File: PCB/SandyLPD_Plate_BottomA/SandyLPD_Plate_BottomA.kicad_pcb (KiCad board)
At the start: 2 copper layers, 131 x 83 mm, 147 parts, among them J1 Conn_02x02_Odd_Even, J2 Conn_01x03, J4 Conn_01x10_Pin, J5 USB_C_Receptacle_USB2.0, J6 USB_C_Receptacle_USB2.0, SW1 BOOT_ALT, SW2 RESET_ALT, SW3 SW_DIP_x04, U1 NCP1117-3.3_SOT223, U3 RP2040, U4 W25Q128JVPIQ, Y1 12MHz

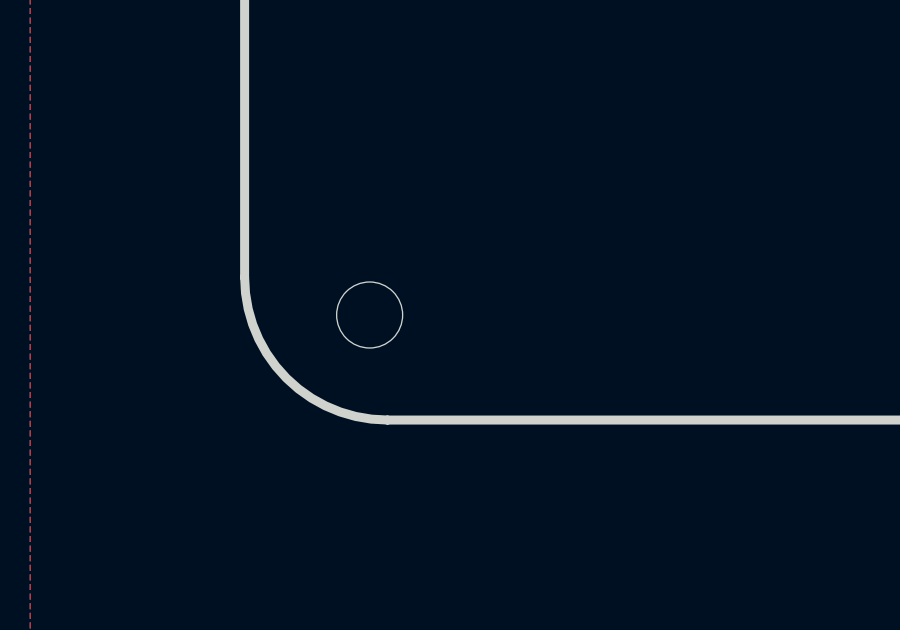
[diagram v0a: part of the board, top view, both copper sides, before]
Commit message: 基板外側のボトム用ネジ位置を変更 #18
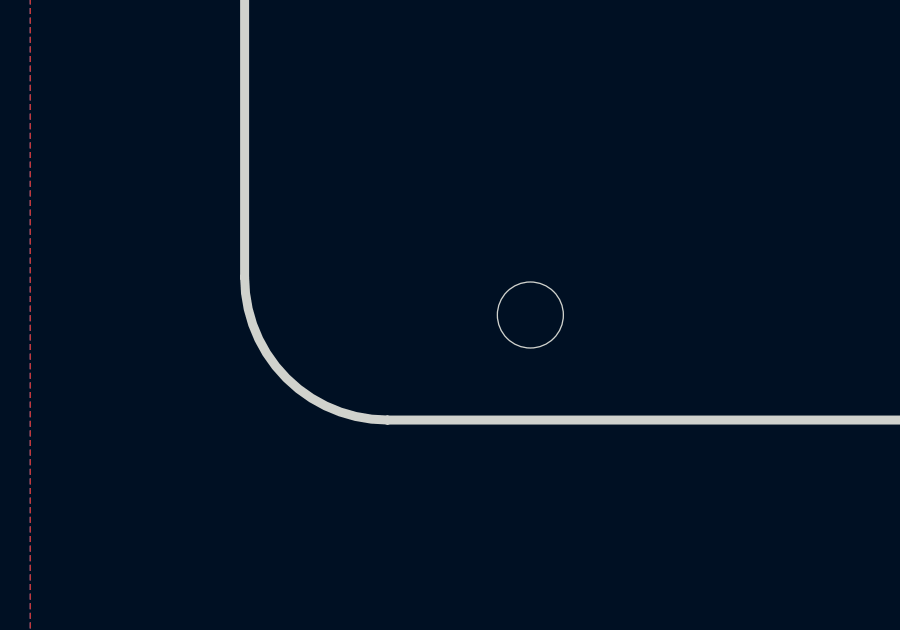
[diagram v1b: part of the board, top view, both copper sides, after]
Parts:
- moved H_btm_3 5.36 mm to (33.0, 111.5)
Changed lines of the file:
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@@
 	(footprint "locallib:MountingHole_2.2mm_M2_no_REF"
 		(layer "B.Cu")
-		(at 27.606876 111.537849 180)
+		(at 32.964693 111.537849 180)
 		(descr "Mounting Hole 2.2mm, no annular, M2")
 		(tags "mounting hole 2.2mm no annular m2")

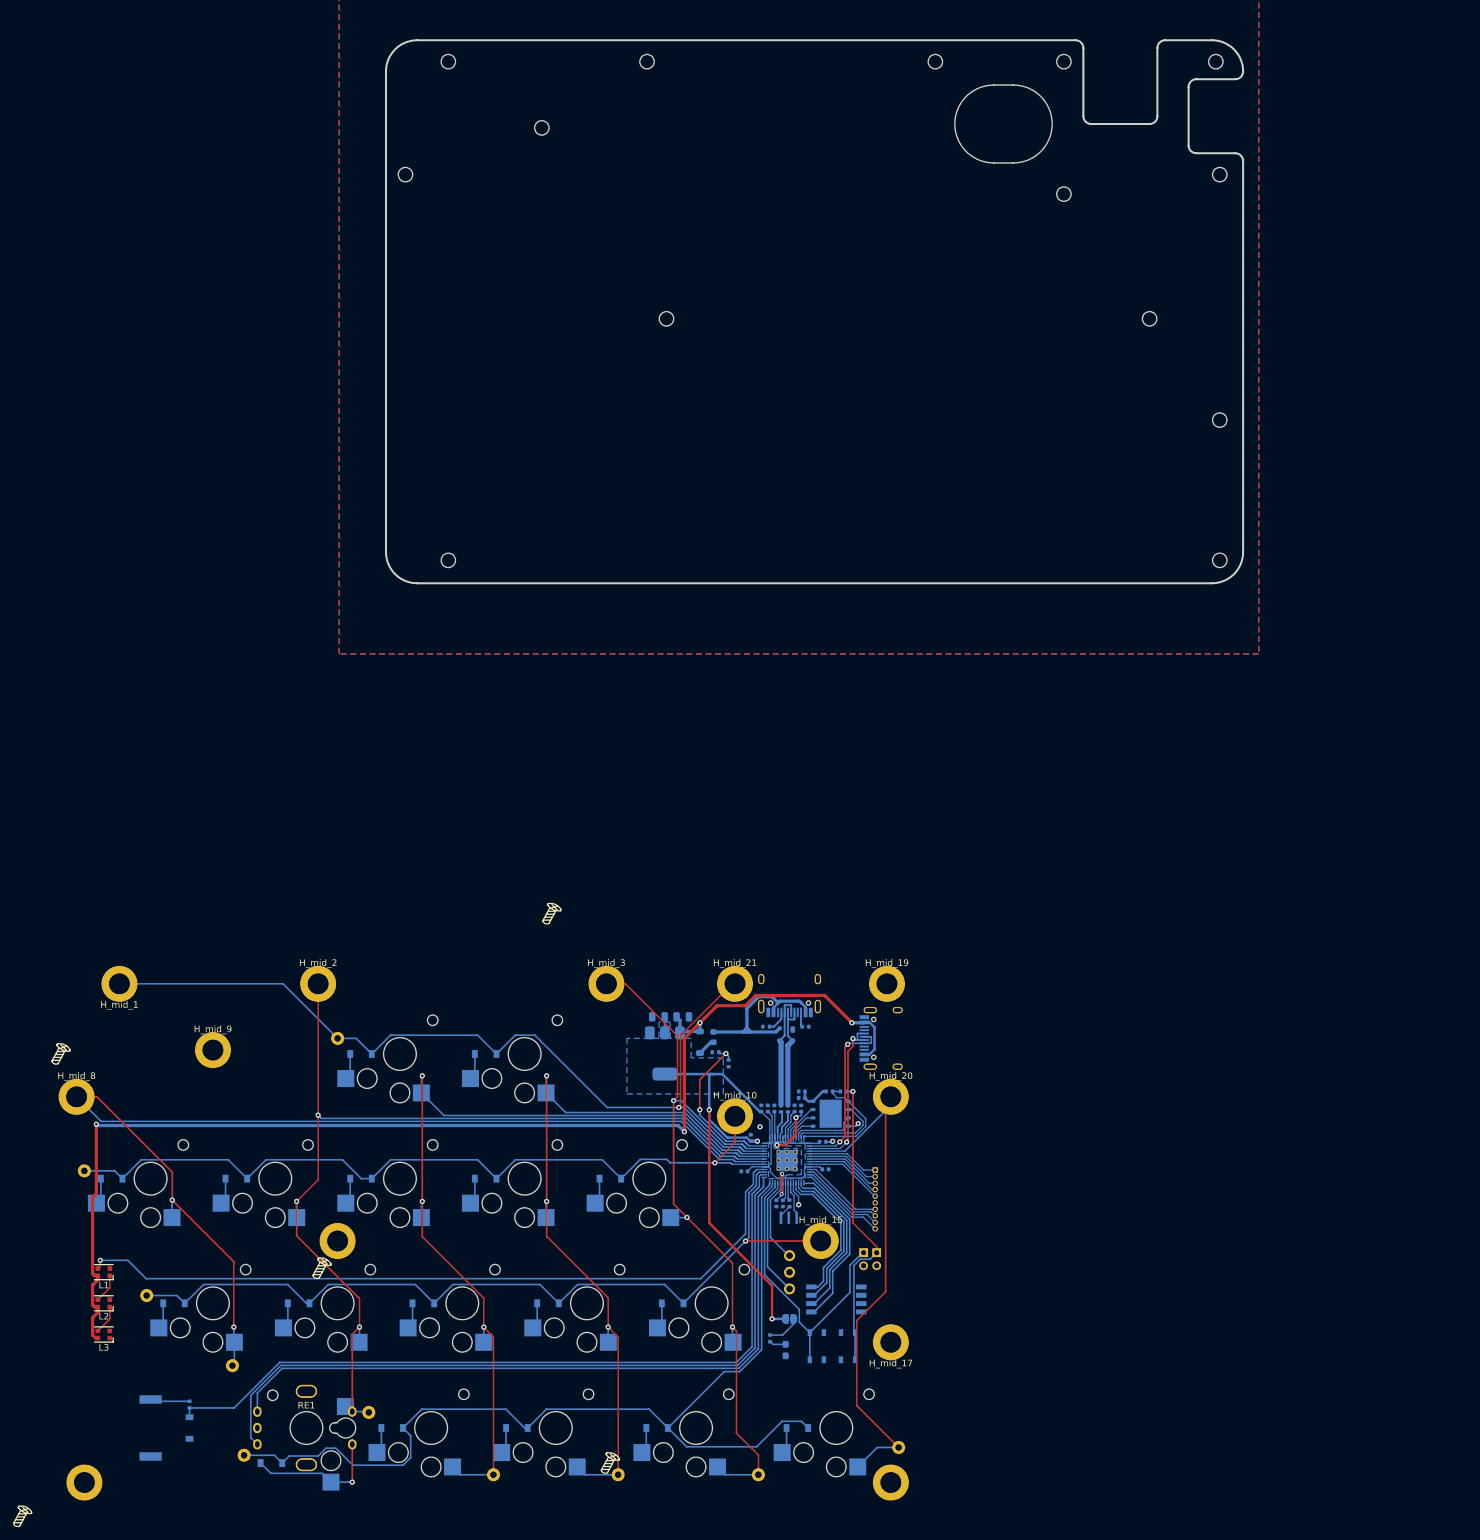
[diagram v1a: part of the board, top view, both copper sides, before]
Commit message: ボトムプレートの左右幅調整 #18
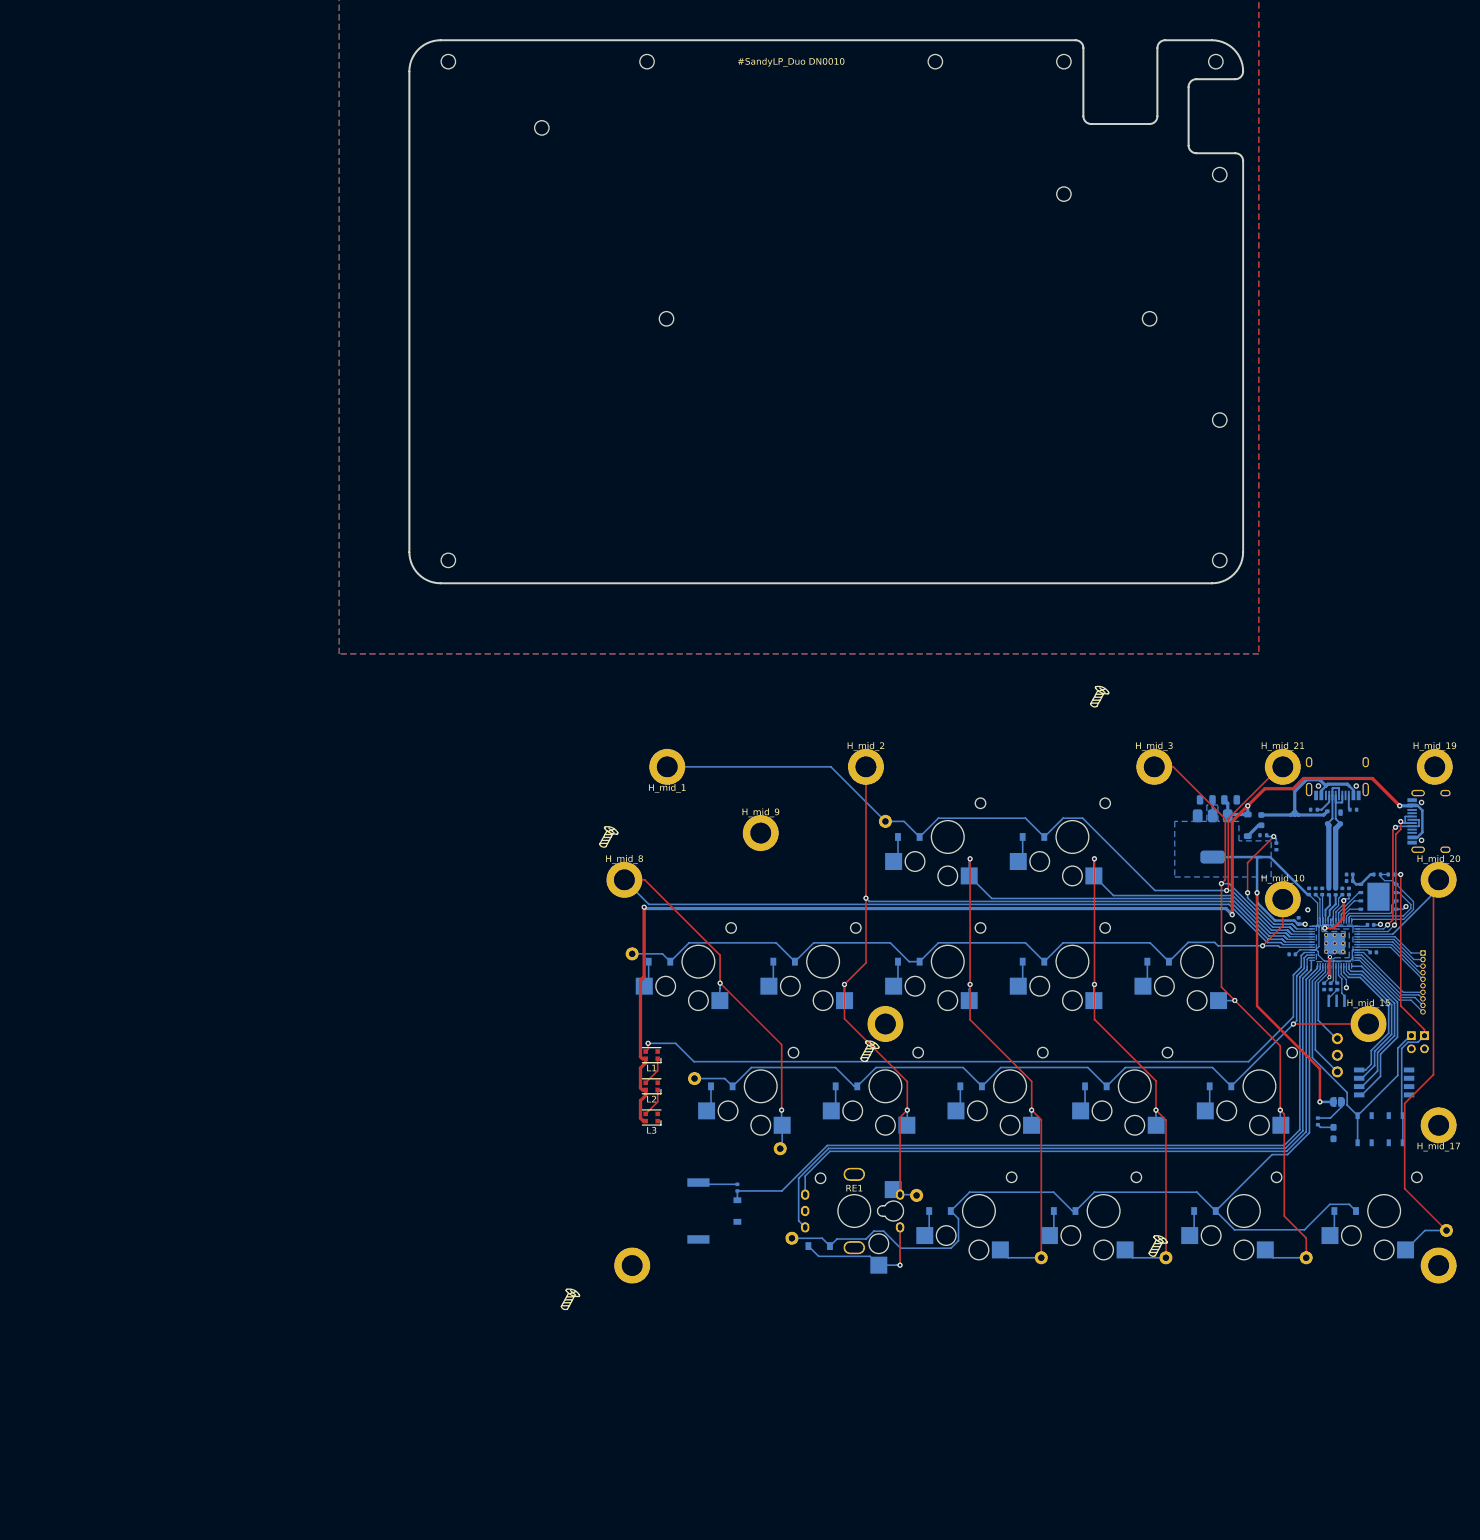
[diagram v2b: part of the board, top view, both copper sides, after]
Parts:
- removed the H_mid_8 at (26.4, 52.6)
- REF**: footprint locallib:SandyLP-Duo_outline_BottomA_with_hole2 -> locallib:SandyLP-Duo_outline_BottomA_with_hole2_narrow_edge
- moved D25 90.0 mm to (108.1, 211.0)
- moved D26 90.0 mm to (127.1, 211.0)
- moved D27 90.0 mm to (148.6, 211.0)
- moved J4 90.0 mm to (181.9, 171.5)
- moved R4 90.0 mm to (174.9, 159.5)
- moved REF** 90.0 mm to (144.4, 134.2)
- moved STLED1 90.0 mm to (168.2, 199.0)
- moved SW3 90.0 mm to (176.0, 191.3)
- moved SW_16 90.0 mm to (99.8, 191.9)
- moved SW_17 90.0 mm to (118.8, 191.9)
- moved T_L_C4 90.0 mm to (164.0, 218.1)
- moved D15 90.0 mm to (74.8, 191.9)
- moved D16 90.0 mm to (93.8, 191.9)
- moved D17 90.0 mm to (112.9, 191.9)
- moved D18 90.0 mm to (131.9, 191.9)
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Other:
- board size 131 x 83 mm -> 127.4 x 83 mm
- board text added: "#SandyLP_Duo DN0010"
- board text removed: "#SandyLP_kbd DN0010, Base by @jpskenn github.com/jpskenn/SandyLP"

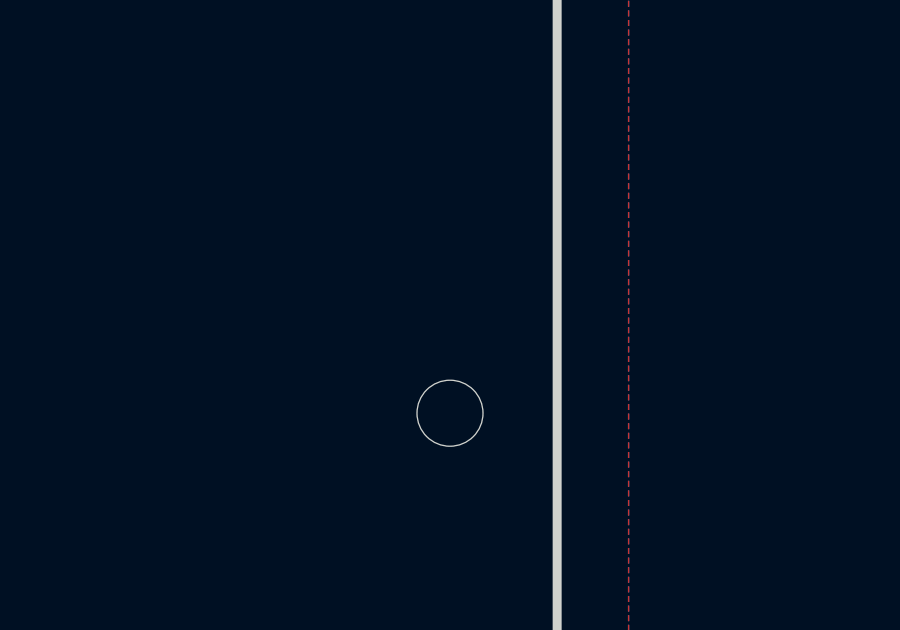
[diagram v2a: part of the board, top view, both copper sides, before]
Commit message: Base→MId中央のネジ位置を1箇所変更
Mid中央をリバーシブルにすると、ソケットのパッドと干渉が出たため。
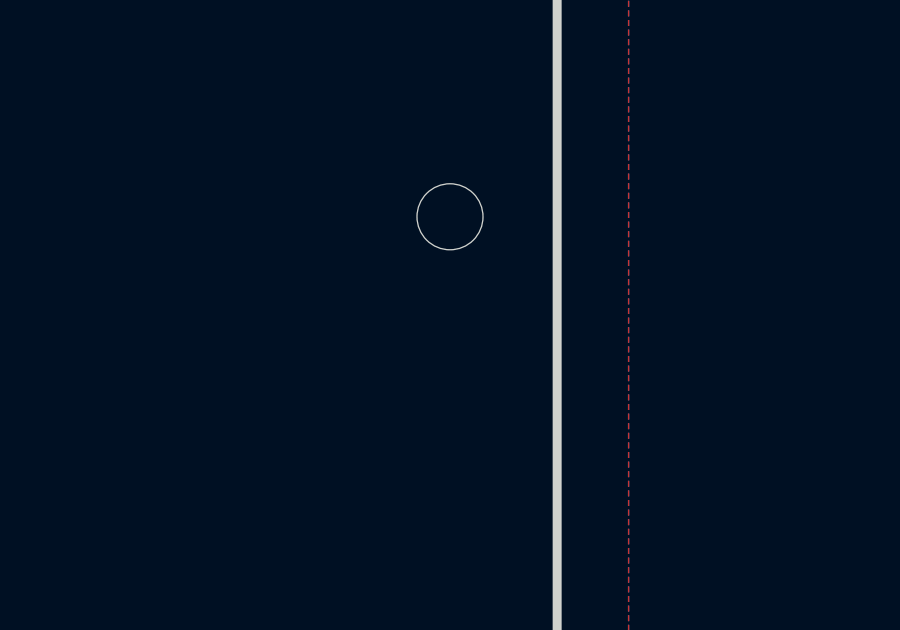
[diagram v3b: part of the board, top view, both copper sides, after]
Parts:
- moved H_mid_17 6.55 mm to (150.8, 83.6)
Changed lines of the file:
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@@
 	(footprint "locallib:MountingHole_2.2mm_M2_no_REF"
 		(layer "F.Cu")
-		(at 150.836667 90.106221 180)
+		(at 150.836667 83.558138 180)
 		(descr "Mounting Hole 2.2mm, no annular, M2")
 		(tags "mounting hole 2.2mm no annular m2")
